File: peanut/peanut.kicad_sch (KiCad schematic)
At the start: 42 parts, among them J1 USB-C, Q1 NMOS, U2 MS5611-01BA, U3 ESP32-C3FH4, Y1 32.768kHz, Y2 40MHz

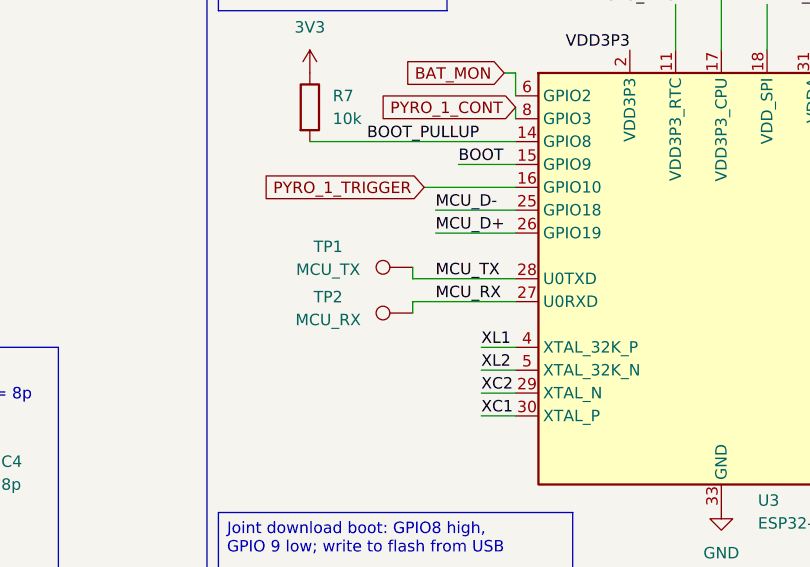
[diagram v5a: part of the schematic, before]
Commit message: bug: Fix missing connections to START/PANIC LEDs
The START/PANIC LEDs now take over the UART interface. If UART is
needed, using the pads of the LEDS should not be functionally different
than using the test points.
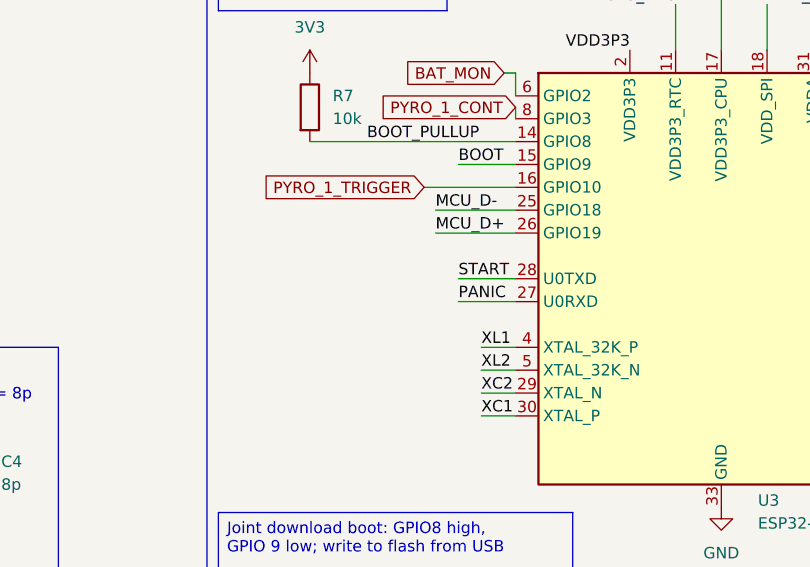
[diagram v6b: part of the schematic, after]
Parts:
- removed TP1: MCU_TX, TestPoint:TestPoint_Pad_D1.0mm, symbol Connector:TestPoint
- removed TP2: MCU_RX, TestPoint:TestPoint_Pad_D1.0mm, symbol Connector:TestPoint
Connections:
- net MCU_RX is gone; now on net PANIC: U3.27 (U0RXD)
- net MCU_TX is gone; now on net START: U3.28 (U0TXD)
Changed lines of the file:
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@@
-	(wire
-		(pts
-			(xy 110.49 96.52) (xy 110.49 97.79)
-		)
-		(stroke
-			(width 0)
-			(type default)
-		)
-	)
 	(wire
 		(pts
@@
 	(wire
 		(pts
-			(xy 110.49 92.71) (xy 110.49 93.98)
-		)
-		(stroke
-			(width 0)
-			(type default)
-		)
-	)
-	(wire
-		(pts
 			(xy 144.78 60.96) (xy 144.78 68.58)
 		)
@@
 	(wire
 		(pts
-			(xy 110.49 93.98) (xy 121.92 93.98)
+			(xy 115.57 93.98) (xy 121.92 93.98)
 		)
 		(stroke
@@
 	(wire
 		(pts
-			(xy 121.92 96.52) (xy 110.49 96.52)
+			(xy 121.92 96.52) (xy 115.57 96.52)
 		)
 		(stroke
@@
 		)
 	)
+	(label "PANIC"
+		(at 115.57 96.52 0)
+		(effects
+			(font
+				(size 1.27 1.27)
+			)
+			(justify left bottom)
+		)
+	)
 	(label "XC2"
 		(at 118.11 106.68 0)
@@
 		)
 	)
-	(label "MCU_TX"
-		(at 113.03 93.98 0)
-		(effects
-			(font
-				(size 1.27 1.27)
-			)
-			(justify left bottom)
-		)
-	)
-	(label "MCU_RX"
-		(at 113.03 96.52 0)
-		(effects
-			(font
-				(size 1.27 1.27)
-			)
-			(justify left bottom)
-		)
-	)
 	(label "I2C_SDA"
 		(at 88.9 177.8 0)
@@
 	(label "MCU_D-"
 		(at 113.03 86.36 0)
+		(effects
+			(font
+				(size 1.27 1.27)
+			)
+			(justify left bottom)
+		)
+	)
+	(label "START"
+		(at 115.57 93.98 0)
 		(effects
 			(font
@@
 	)
 	(symbol
-		(lib_id "Connector:TestPoint")
-		(at 110.49 97.79 90)
-		(unit 1)
-		(body_style 1)
-		(exclude_from_sim no)
-		(in_bom yes)
-		(on_board yes)
-		(in_pos_files yes)
-		(dnp no)
-		(property "Reference" "TP2"
-			(at 101.092 96.012 90)
-			(show_name no)
-			(do_not_autoplace no)
-			(effects
-				(font
-					(size 1.27 1.27)
-				)
-			)
-		)
-		(property "Value" "MCU_RX"
-			(at 101.092 98.552 90)
-			(show_name no)
-			(do_not_autoplace no)
-			(effects
-				(font
-					(size 1.27 1.27)
-				)
-			)
-		)
-		(property "Footprint" "TestPoint:TestPoint_Pad_D1.0mm"
-			(at 110.49 92.71 0)
-			(hide yes)
-			(show_name no)
-			(do_not_autoplace no)
-			(effects
-				(font
-					(size 1.27 1.27)
-				)
-			)
-		)
-		(property "Datasheet" ""
-			(at 110.49 92.71 0)
-			(hide yes)
-			(show_name no)
-			(do_not_autoplace no)
-			(effects
-				(font
-					(size 1.27 1.27)
-				)
-			)
-		)
-		(property "Description" "test point"
-			(at 110.49 97.79 0)
-			(hide yes)
-			(show_name no)
-			(do_not_autoplace no)
-			(effects
-				(font
-					(size 1.27 1.27)
-				)
-			)
-		)
-		(property "MPN" "-"
-			(at 110.49 97.79 90)
-			(hide yes)
-			(show_name no)
-			(do_not_autoplace no)
-			(effects
-				(font
-					(size 1.27 1.27)
-				)
-			)
-		)
-		(pin "1"
-		)
-		(instances
-			(project "peanut"
-				(path "/5c6b6cfc-6c84-425a-9b66-e6111713aae8"
-					(reference "TP2")
-					(unit 1)
-				)
-			)
-		)
-	)
-	(symbol
 		(lib_id "power:GND")
 		(at 107.95 187.96 0)
@@
 					(unit 1)
 				)
-			)
-		)
-	)
-	(symbol
-		(lib_id "Connector:TestPoint")
-		(at 110.49 92.71 90)
-		(unit 1)
-		(body_style 1)
-		(exclude_from_sim no)
-		(in_bom yes)
-		(on_board yes)
-		(in_pos_files yes)
-		(dnp no)
-		(property "Reference" "TP1"
-			(at 101.092 90.424 90)
-			(show_name no)
-			(do_not_autoplace no)
-			(effects
-				(font
-					(size 1.27 1.27)
-				)
-			)
-		)
-		(property "Value" "MCU_TX"
-			(at 101.092 92.964 90)
-			(show_name no)
-			(do_not_autoplace no)
-			(effects
-				(font
-					(size 1.27 1.27)
-				)
-			)
-		)
-		(property "Footprint" "TestPoint:TestPoint_Pad_D1.0mm"
-			(at 110.49 87.63 0)
-			(hide yes)
-			(show_name no)
-			(do_not_autoplace no)
-			(effects
-				(font
-					(size 1.27 1.27)
-				)
-			)
-		)
-		(property "Datasheet" ""
-			(at 110.49 87.63 0)
-			(hide yes)
-			(show_name no)
-			(do_not_autoplace no)
-			(effects
-				(font
-					(size 1.27 1.27)
-				)
-			)
-		)
-		(property "Description" "test point"
-			(at 110.49 92.71 0)
-			(hide yes)
-			(show_name no)
-			(do_not_autoplace no)
-			(effects
-				(font
-					(size 1.27 1.27)
-				)
-			)
-		)
-		(property "MPN" "-"
-			(at 110.49 92.71 90)
-			(hide yes)
-			(show_name no)
-			(do_not_autoplace no)
-			(effects
-				(font
-					(size 1.27 1.27)
-				)
-			)
-		)
-		(pin "1"
-		)
-		(instances
-			(project "peanut"
-				(path "/5c6b6cfc-6c84-425a-9b66-e6111713aae8"
-					(reference "TP1")
-					(unit 1)
-				)

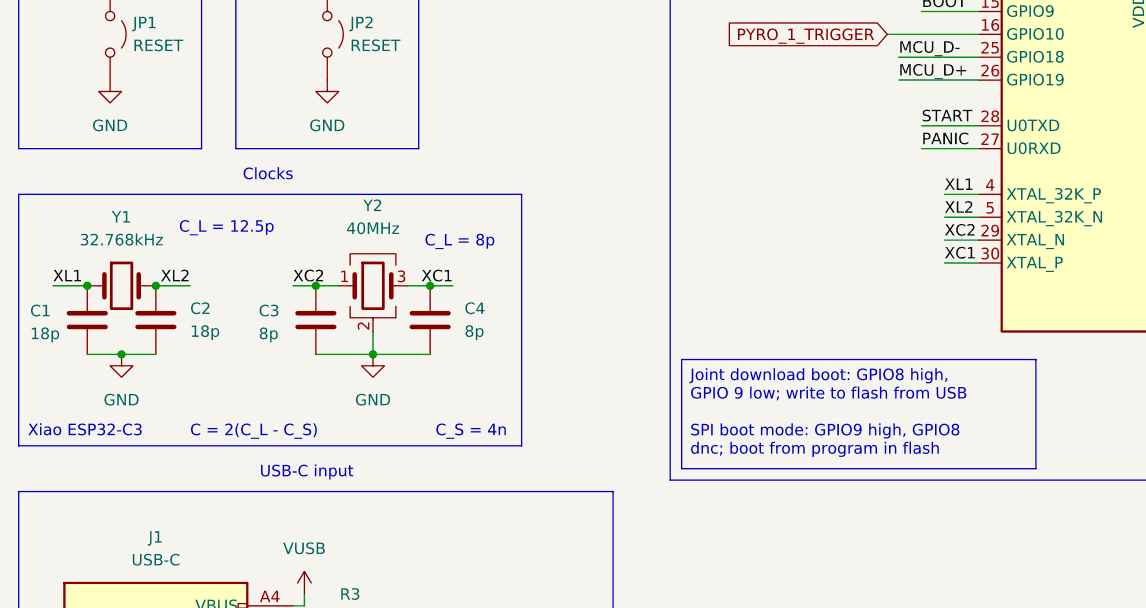
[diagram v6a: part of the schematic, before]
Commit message: feat: Remove secondary crystal oscillator
We will rely on the internal crystal oscillator: it is cheaper, saves me
headaches routing the RF stuff and removes an unnecessary component.
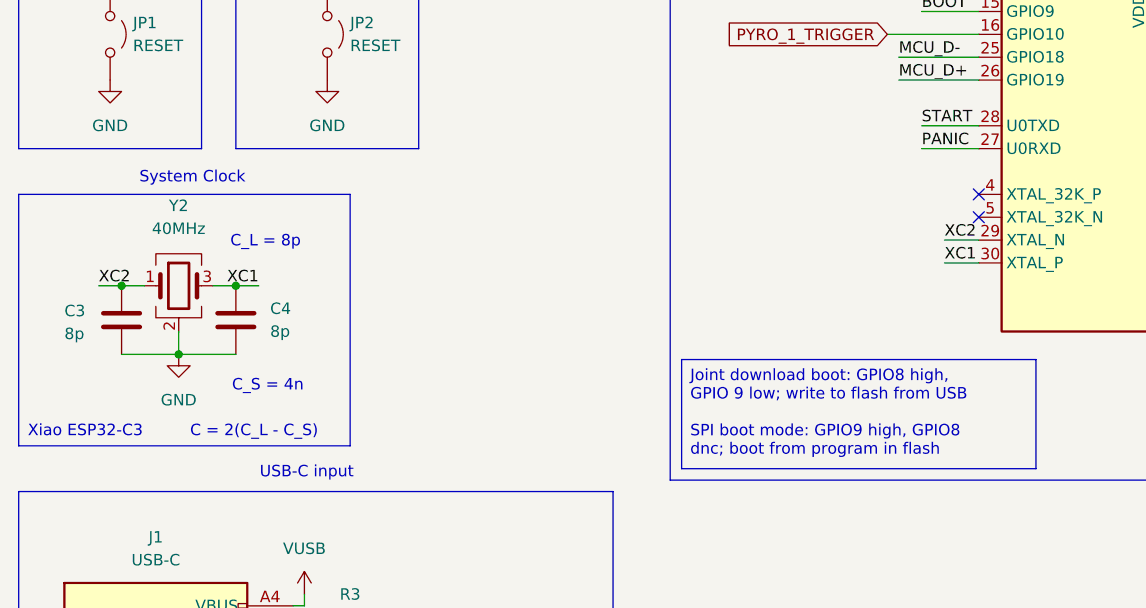
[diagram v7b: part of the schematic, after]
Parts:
- removed C1, C2: 18p, Capacitor_SMD:C_0402_1005Metric, symbol Device:C
- removed Y1: 32.768kHz, Crystal:Crystal_SMD_MicroCrystal_CM9V-T1A-2Pin_1.6x1.0mm, symbol Device:Crystal
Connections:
- net XL1: no longer names the net of U3.4 (XTAL_32K_P)
- net XL2: no longer names the net of U3.5 (XTAL_32K_N)
- no-connect marks 9 -> 11
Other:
- note added: "System Clock"
- note removed: "C_L = 12.5p"
- note removed: "Clocks"
- moved on the sheet: C3, C4, Y2

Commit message: bug: Buzzer not connected
Fixed the buzzer line not being connected to anything by replacing the
PANIC LED with it. Buzzing during panic is equally acceptable, if not
annoying, while debugging.
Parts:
- removed D2: RED, LED_SMD:LED_0805_2012Metric, symbol Device:LED
- removed R9: 330R, Resistor_SMD:R_0402_1005Metric, symbol Device:R
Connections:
- net PANIC is gone; now on net BUZ_PWM: U3.27 (U0RXD)
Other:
- note added: "LED boot indicator"
- note removed: "LED indicators"
